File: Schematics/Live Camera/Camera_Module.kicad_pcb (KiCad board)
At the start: 2 copper layers, 69.5 x 60 mm, 96 parts, among them J1 Stack Male Edge Connector, J2 SWD_01x04_Pin, J3 USB_C_Female_USB2_Small, J4 Screw_Terminal_01x02, J5 VTX_DAT, J6 CAM_PWR, J7 CAM_DAT, J8 VTX_PWR, Q1 AO3400A, Q2 AO3401A, Q3 AO3400A, Q4 AO3400A, Q5 AO3401A, SW1 SW_STM_RESET, SW2 SW_STM_BOOT_MODE, U1 LM66100DCKR, U10 AMS1117-3.3, U11 CP2102N-Axx-xQFN28, U2 ACS70331EOLC, U3 STM32F103CBT6, U5 LM66100DCKR, U6 LM66100DCKR, U7 ISO1042BDWVR, U8 W25Q128JVS, Y1 X322516MMB4SI

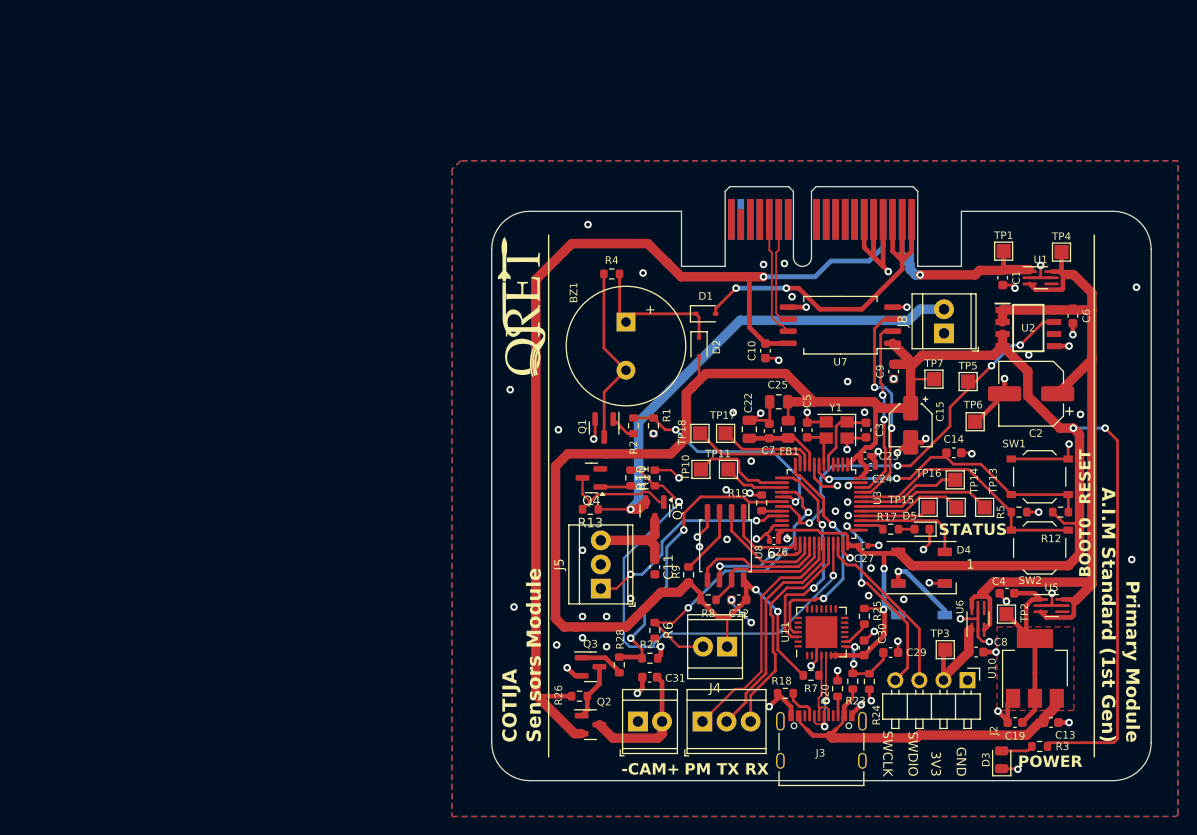
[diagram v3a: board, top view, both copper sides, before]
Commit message: Updated Camera Layout
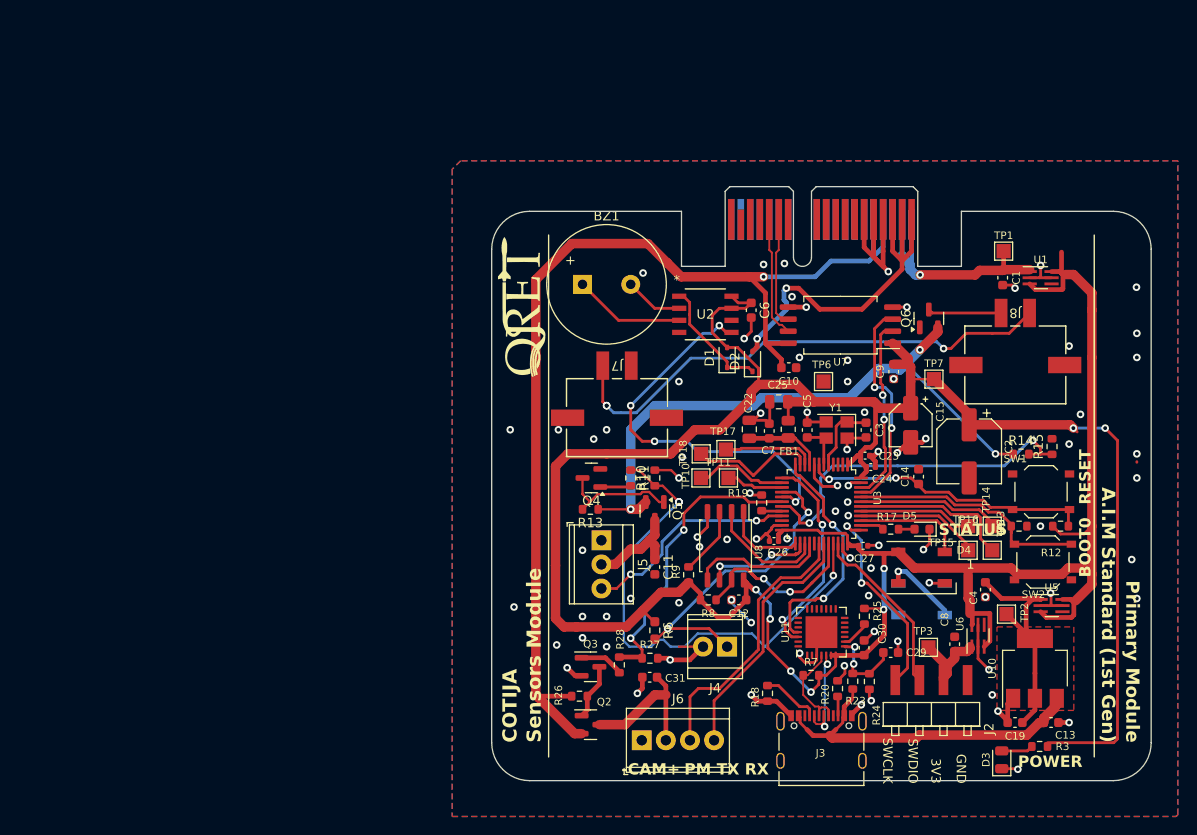
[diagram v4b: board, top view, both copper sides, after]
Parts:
- removed Q1: AO3400A, Package_TO_SOT_SMD:SOT-23
- removed R1: 10k, Resistor_SMD:R_0603_1608Metric
- removed R2: 510R, Resistor_SMD:R_0603_1608Metric
- removed R4: 1k, Resistor_SMD:R_0603_1608Metric
- removed TP4: TP_MUX, TestPoint:TestPoint_Pad_1.5x1.5mm
- removed TP5: TP_ISENSE, TestPoint:TestPoint_Pad_1.5x1.5mm
- added Q6: AO3401A, Package_TO_SOT_SMD:SOT-23, F.Cu at (133.0, 59.4)
- added R14: 100k, Resistor_SMD:R_0603_1608Metric, F.Cu at (142.7, 73.7)
- added R15: 20k, Resistor_SMD:R_0603_1608Metric, F.Cu at (146.0, 72.9)
- BZ1: value PKM13EPYH4000 -> PS1240P02BT
- C6: value 0.1uF -> 100nF
- J2: footprint SWD_Header:SWD_PinHeader_1x04_P2.54mm_Horizontal -> SWD_Header:SWD_PinHeader_1x04_P2.54mm_Horizontal_SMD
- J4: value Screw_Terminal_01x02 -> Therm_In
- J5: value VTX_DAT -> VTX
- J6: value CAM_PWR -> RunCam6; footprint TerminalBlock_TE-Connectivity:TerminalBlock_TE_282834-2_1x02_P2.54mm_Horizontal -> TerminalBlock_TE-Connectivity:TerminalBlock_TE_282834-4_1x04_P2.54mm_Horizontal
- J7: value CAM_DAT -> VTX_BATT_IN; footprint TerminalBlock_TE-Connectivity:TerminalBlock_TE_282834-3_1x03_P2.54mm_Horizontal -> footprints:CONN_2-1445057-2_TYCO
- J8: value VTX_PWR -> VTX_BATT_SWITCH; footprint TerminalBlock_TE-Connectivity:TerminalBlock_TE_282834-2_1x02_P2.54mm_Horizontal -> footprints:CONN_2-1445057-2_TYCO
- R11: value 820 -> 510
- R6: footprint Resistor_SMD:R_0603_1608Metric -> Resistor_SMD:R_0603_1608Metric_Pad0.98x0.95mm_HandSolder
- U2: value ACS70331EOLC -> TPM8837C-SO1R; footprint footprints:SOIC127P600X175-8N -> footprints:SOP-8_TPK
- moved J7 38.2 mm to (101.7, 64.4), turned to 180 degrees
- moved U2 34.1 mm to (109.5, 59.0)
- moved C6 33.9 mm to (114.3, 58.5)
- moved TP6 16.5 mm to (121.9, 66.0)
- moved J8 9.26 mm to (143.6, 58.8), turned to 180 degrees
- moved C2 8.92 mm to (137.3, 73.4), turned to -90 degrees
- moved BZ1 6.44 mm to (95.2, 55.8), turned to 0 degrees
- moved TP16 6.25 mm to (139.7, 81.3)
- moved TP15 6.18 mm to (137.2, 83.8)
- moved D2 5.84 mm to (114.4, 63.9), turned to 90 degrees
- moved D1 5.13 mm to (111.8, 63.5), turned to 90 degrees
- moved J5 5.09 mm to (98.5, 82.8), turned to -90 degrees
- moved TP13 4.59 mm to (139.7, 83.8)
- moved C14 4.48 mm to (131.9, 76.1), turned to 90 degrees
- moved C10 3.03 mm to (118.3, 64.6), turned to 180 degrees
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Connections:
- C11 pad 1: VTX_BAT -> VTX_V+
- C12 pad 1: +3.3V -> V_MUX
- C15 pad 1: +3.3V -> V_MUX
- C23 pad 1: +3.3V -> V_MUX
- C24 pad 1: +3.3V -> V_MUX
- C25 pad 1: +3.3V -> V_MUX
- C26 pad 1: +3.3V -> V_MUX
- C27 pad 1: +3.3V -> V_MUX
- C30 pad 2: +3.3V -> V_MUX
- C9 pad 2: +3.3V -> V_MUX
- D1 pad 1: Net-(BZ1--) -> Net-(D1-K)
- D1 pad 2: +BATT -> V_MUX
- D2 pad 1: Net-(BZ1--) -> Net-(D1-K)
- D2 pad 2: +3.3V -> +BATT
- D4 pad 1: +3.3V -> V_MUX
- D6 pad 1: +3.3V -> V_MUX
- FB1 pad 2: +3.3V -> V_MUX
- J4 pad 1: +3.3V -> V_THERM
- J4 pad 2: V_THERM -> GND
- J5 pad 1: VTX_DATA -> GND
- J5 pad 2: GND -> VTX_V+
- J5 pad 3: VTX_BAT -> VTX_DATA
- J7 pad 1: CAM_TX -> GND
- J7 pad 2: CAM_RX -> Net-(J7-Pad2)
- J8 pad 1: GND -> Net-(J7-Pad2)
- J8 pad 2: VTX_8V -> Net-(Q6-D)
- Q5 pad 2: VTX_8V -> VTX_BATT
- Q5 pad 3: VTX_BAT -> VTX_V+
- R12 pad 2: +3.3V -> V_MUX
- R13 pad 1: VTX_8V -> VTX_BATT
- R25 pad 2: +3.3V -> V_MUX
- R3 pad 2: +3.3V -> V_MUX
- R6 pad 1: V_THERM -> V_MUX
- R6 pad 2: GND -> V_THERM
- R7 pad 1: +3.3V -> V_MUX
- R8 pad 2: +3.3V -> V_MUX
- R9 pad 2: +3.3V -> V_MUX
- SW2 pad 2: +3.3V -> V_MUX
- TP7 pad 1: +3.3V -> V_MUX
- U11 pad 6: +3.3V -> V_MUX
- U11 pad 7: +3.3V -> V_MUX
- U2 pad 1: V_MUX -> Net-(D1-K)
- U2 pad 2: V_MUX -> Net-(BZ1-+)
- U2 pad 3: +3.3V -> Net-(BZ1--)
- U2 pad 4: +3.3V -> GND
- U2 pad 5: GND -> BUZZER_B
- U2 pad 6: unconnected-(U2-NC-Pad6) -> BUZZER_A
- U2 pad 7: CURR_SENSE -> V_MUX
- U3 pad 1: +3.3V -> V_MUX
- U3 pad 17: BUZZER -> BUZZER_B
- U3 pad 19: CURR_SENSE -> VTX_BATT_SENSE
- U3 pad 24: +3.3V -> V_MUX
- U3 pad 29: RESET_FL -> BUZZER_A
- U3 pad 32: CAM_PWM -> RESET_FL
- U3 pad 36: +3.3V -> V_MUX
- U3 pad 48: +3.3V -> V_MUX
- U7 pad 1: +3.3V -> V_MUX
- U8 pad 8: +3.3V -> V_MUX
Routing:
- net +3.3V: track 277.0 -> 0.00 mm, vias 6 -> 0
- net V_MUX: track 87.1 -> 340.1 mm, vias 0 -> 8
- net VTX_BATT: track 0.00 -> 66.6 mm, vias 0 -> 5
- net Net-(J7-Pad2): track 0.00 -> 54.2 mm, vias 0 -> 3
- net VTX_8V: track 52.0 -> 0.00 mm, vias 1 -> 0
- net CURR_SENSE: track 42.9 -> 0.00 mm, vias 4 -> 0
- net BUZZER_B: track 0.00 -> 41.2 mm, vias 0 -> 4
- net VTX_BATT_SENSE: track 0.00 -> 37.8 mm, vias 0 -> 2
- net BUZZER: track 24.4 -> 0.00 mm, vias 2 -> 0
- net CAM_PWM: track 23.6 -> 0.00 mm
- net GND: track 134.5 -> 121.3 mm, vias 84 -> 82
- net Net-(BZ1-+): track 19.1 -> 6.15 mm
- net Net-(D1-K): track 0.00 -> 12.7 mm
- net VTX_BAT: track 11.8 -> 0.00 mm
- net VTX_V+: track 0.00 -> 10.8 mm
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
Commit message: Tweaks + 3D model additions
Added/tweaked some notes in the schematic, adjusted silkscreen on PCB + added "PB-FREE" label, updated SWD footprint, and added all missing 3D models to project.
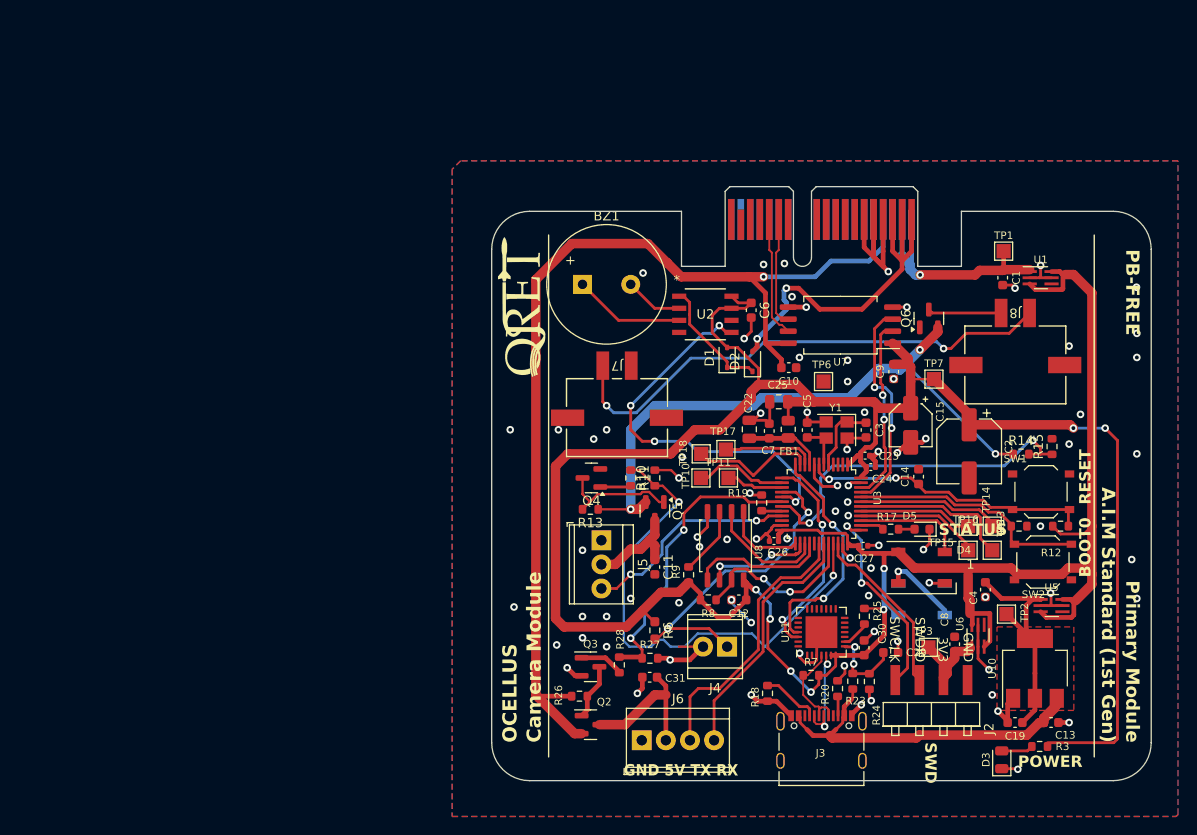
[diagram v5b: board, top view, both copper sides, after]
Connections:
- net 5V_RAW renamed 5V_USB
- net V_MUX renamed +3.3V
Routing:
- net +3.3V: track 340.1 -> 336.3 mm
- net RESET_FL: track 19.0 -> 18.4 mm
- net VTX_PWR: vias 4 -> 2
- net VTX_BATT: vias 5 -> 3
- net Net-(J7-Pad2): vias 3 -> 2
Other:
- board text added: "Camera Module"
- board text added: "GND 5V TX RX"
- board text added: "OCELLUS"
- board text added: "Ocellus Rev 1.0 QRET Feb 2025 Ethan Toste Kennan Bays Noah Del Rizzo Fedor Kim"
- board text added: "PB-FREE"
- board text removed: "-CAM+"
- board text removed: "?????? Rev 1.0 QRET Feb 2025 Ethan Toste Kennan Bays Noah Del Rizzo Fedor Kim"
- board text removed: "COTIJA"
- board text removed: "JLCJLCJLCJLC"
- board text removed: "PM TX RX"
- board text removed: "Sensors Module"

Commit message: Refined & finalized PCB layout
Moved connectors all to the edge of the PCB to make access easier, beefed up several traces, optimized trace paths to minimize traces on the rear ground plane. Removed a few redundant test points too.
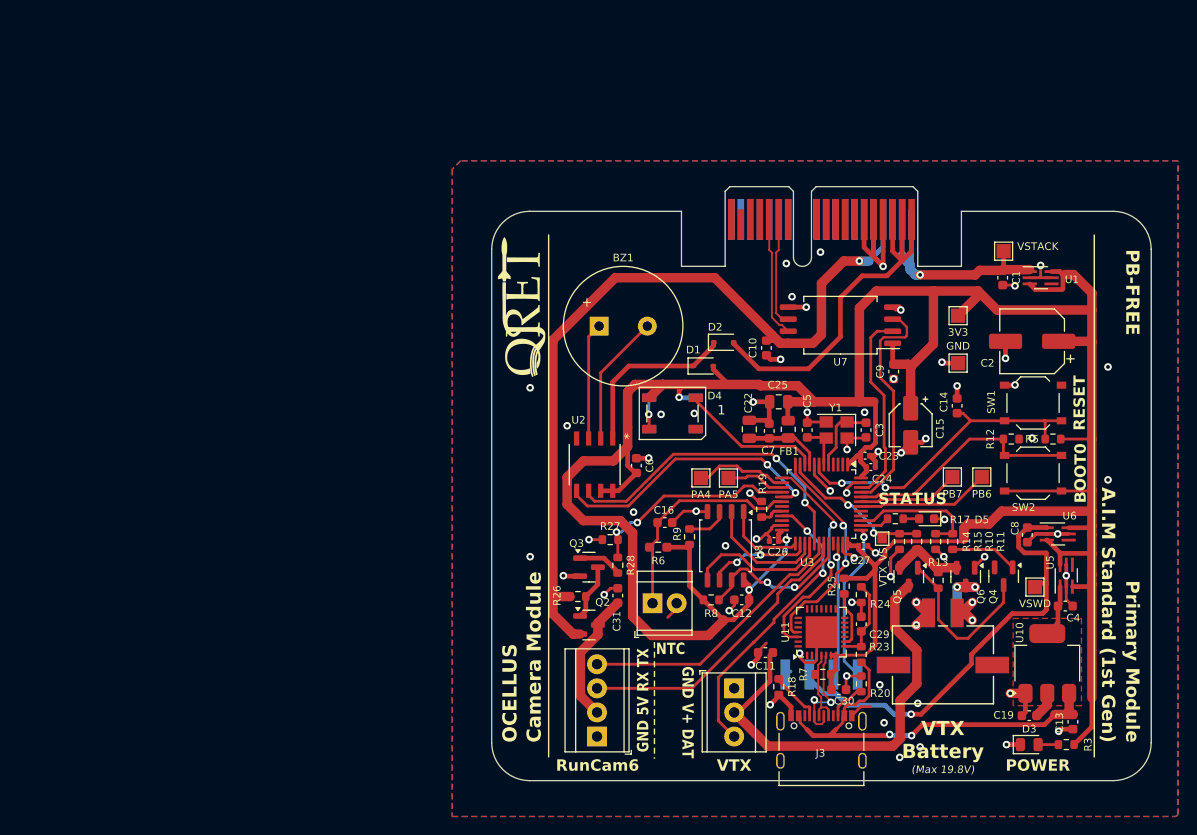
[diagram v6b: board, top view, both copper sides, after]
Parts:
- removed TP14: PB5, TestPoint:TestPoint_Pad_1.5x1.5mm
- removed TP15: PB4, TestPoint:TestPoint_Pad_1.5x1.5mm
- removed TP17: PA0, TestPoint:TestPoint_Pad_1.5x1.5mm
- removed TP18: PA1, TestPoint:TestPoint_Pad_1.5x1.5mm
- added C16: 100nF, Capacitor_SMD:C_0603_1608Metric, F.Cu at (105.2, 80.9)
- J2, J8: moved to B.Cu
- TP1: value TP_VSTACK -> VSTACK
- TP2: value TP_VUSB -> VTX_VS; footprint TestPoint:TestPoint_Pad_1.5x1.5mm -> TestPoint:TestPoint_Pad_1.0x1.0mm
- TP3: value TP_VSWD -> VSWD
- TP6: value TP_GND -> GND
- TP7: value TP_3V3 -> 3V3
- moved Q4 44.7 mm to (140.9, 86.6), turned to -90 degrees
- moved J7 43.1 mm to (136.0, 90.4)
- moved R13 37.4 mm to (134.0, 87.0), turned to -90 degrees
- moved R11 34.6 mm to (135.5, 82.9)
- moved J8 33.4 mm to (133.0, 90.4), turned to 0 degrees
- moved D6 32.8 mm to (106.0, 69.4), turned to 180 degrees
- moved D4 30.9 mm to (106.0, 69.4)
- moved R10 30.3 mm to (133.7, 82.9), turned to -90 degrees
- moved Q5 27.6 mm to (130.9, 86.6)
- moved Q6 27.5 mm to (136.9, 86.6), turned to -90 degrees
- moved J5 21.0 mm to (112.5, 98.4)
- moved C6 20.4 mm to (102.2, 74.9), turned to 90 degrees
- moved U2 19.7 mm to (97.8, 74.8), turned to -90 degrees
- moved J2 19.2 mm to (117.9, 96.9)
- moved R15 18.9 mm to (129.9, 82.9), turned to -90 degrees
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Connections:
- J6 pad 3: CAM_TX -> CAM_RX
- J6 pad 4: CAM_RX -> CAM_TX
- TP2 pad 1: V_REGUSB -> VTX_BATT_SENSE
- U3 pad 10: Net-(U3-PA0) -> RGB_DATA
- U3 pad 11: Net-(U3-PA1) -> VTX_BATT_SENSE
- U3 pad 16: V_THERM -> CAM_PWR
- U3 pad 18: CAM_PWR -> V_THERM
- U3 pad 19: VTX_BATT_SENSE -> unconnected-(U3-PB1-Pad19)
- U3 pad 33: VTX_PWR -> unconnected-(U3-PA12-Pad33)
- U3 pad 39: RGB_DATA -> VTX_PWR
- U3 pad 40: Net-(U3-PB4) -> unconnected-(U3-PB4-Pad40)
- U3 pad 41: Net-(U3-PB5) -> unconnected-(U3-PB5-Pad41)
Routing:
- net VTX_BATT: track 66.6 -> 7.59 mm, vias 3 -> 0
- net Net-(J7-Pad2): track 54.2 -> 7.20 mm
- net VTX_PWR: track 54.2 -> 13.9 mm, vias 2 -> 0
- net V_SWD: track 8.23 -> 47.2 mm, vias 0 -> 1
- net VTX_V+: track 10.8 -> 46.0 mm
- net BUZZER_A: track 0.00 -> 33.4 mm, vias 0 -> 2
- net +5V: track 114.9 -> 90.5 mm
- net VTX_BATT_SENSE: track 37.8 -> 16.1 mm
- net V_REGUSB: track 25.7 -> 8.33 mm
- net Net-(U3-PA1): track 13.3 -> 0.00 mm
- net Net-(U3-PB4): track 13.1 -> 0.00 mm
- net BUZZER_B: track 41.2 -> 29.1 mm, vias 4 -> 2
- net Net-(U3-PB5): track 12.0 -> 0.00 mm
- net V_THERM: track 33.9 -> 23.7 mm, vias 2 -> 0
- net Net-(U3-PA0): track 9.69 -> 0.00 mm
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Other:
- board text added: "(Max 19.8V)"
- board text added: "GND 5V RX TX"
- board text added: "GND V+ DAT"
- board text added: "NTC"
- board text added: "RunCam6"
- board text added: "VTX"
- board text added: "VTX Battery"
- board text added: "VTX Switch"
- board text removed: "GND 5V TX RX"

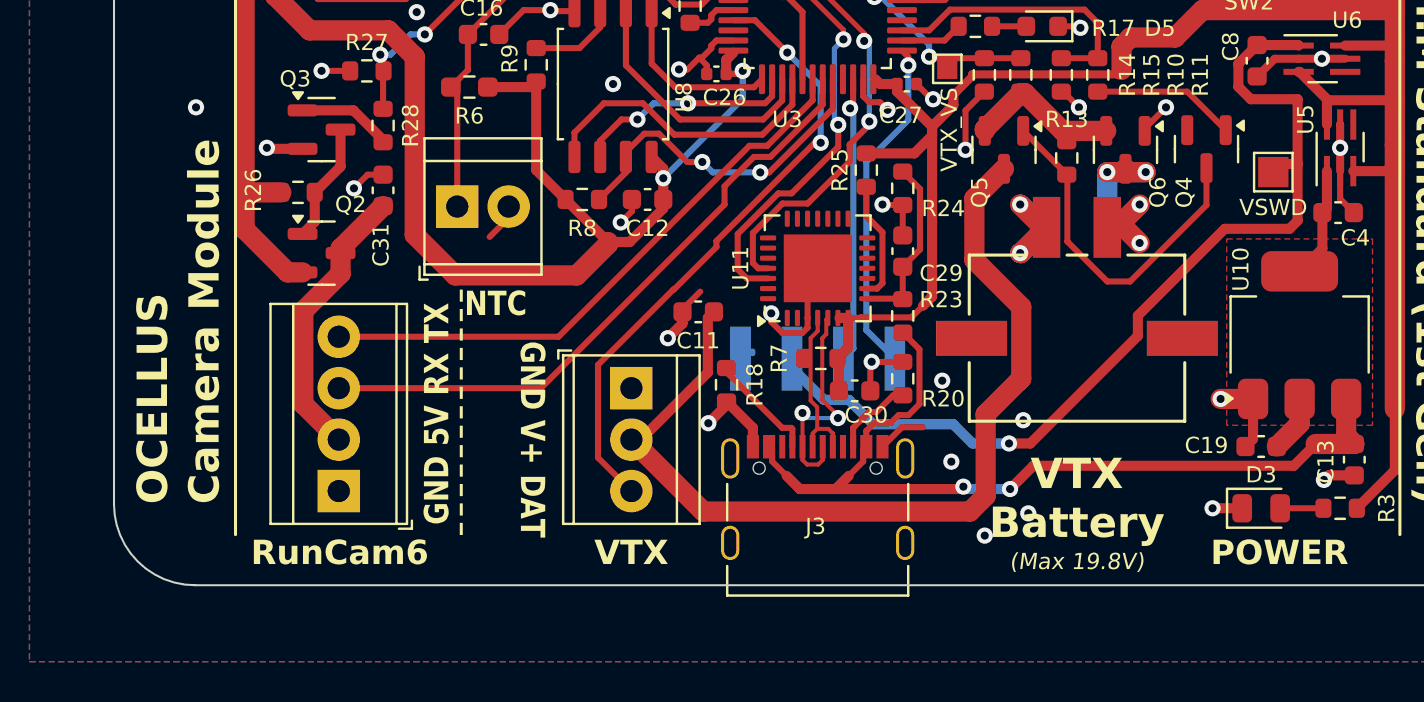
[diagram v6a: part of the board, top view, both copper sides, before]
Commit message: Quick maintenance
- Changed USB-C port to new one (C5178541)
- Moved VTX battery/switch connectors 4mm forward
- Added polarity markers to VTX battery/switch connectors
- Tweaked silkscreen
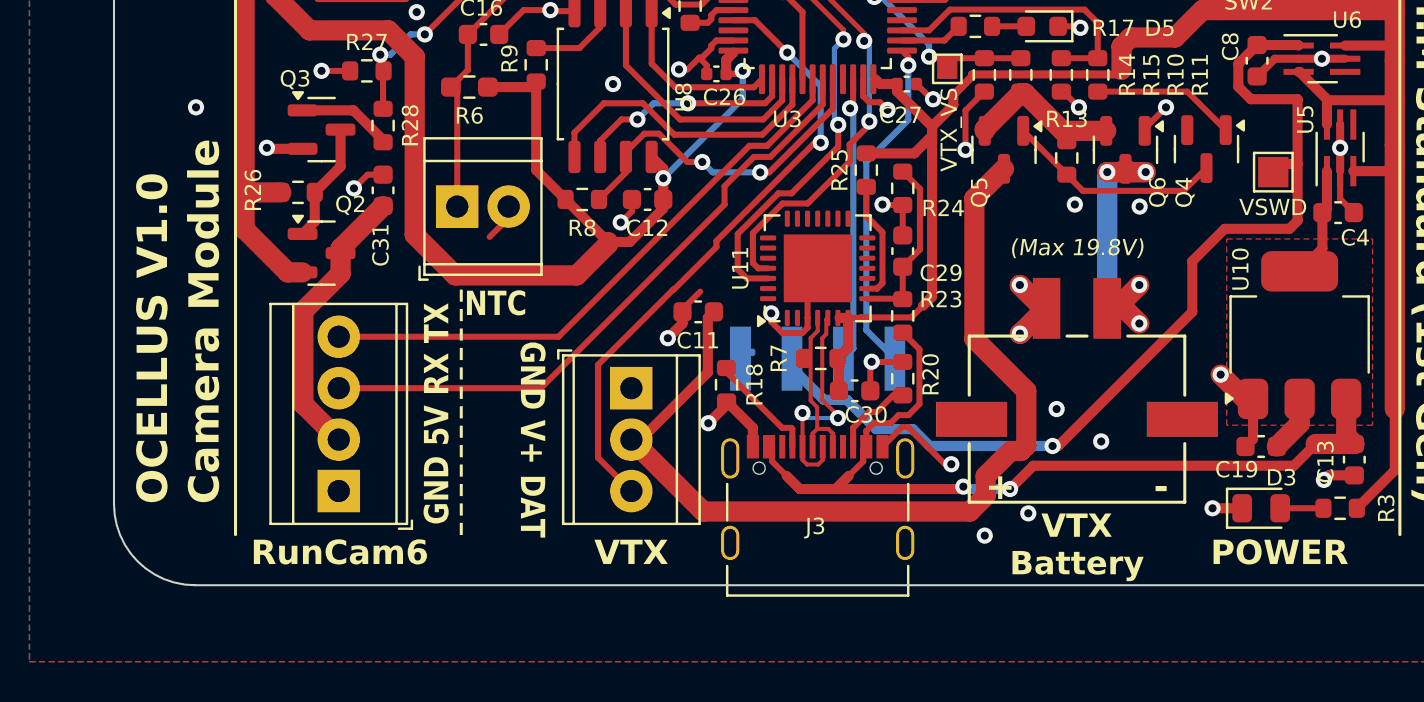
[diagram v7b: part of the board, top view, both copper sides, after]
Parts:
- moved J7 4.00 mm to (136.0, 94.4)
- moved J8 4.00 mm to (133.0, 94.4)
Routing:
- net Net-(Q4-D): track 17.4 -> 10.8 mm
- net Net-(Q6-D): track 6.66 -> 10.7 mm
- net GND: track 128.1 -> 130.8 mm, vias 64 -> 66
- net V_SWD: track 47.2 -> 48.1 mm
- net VTX_V+: track 46.0 -> 46.5 mm
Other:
- board text added: "+ -"
- board text added: "- +"
- board text added: "OCELLUS V1.0"
- board text added: "Ocellus Rev 1.0 QRET Mar 2025 Ethan Toste Kennan Bays Noah Del Rizzo Fedor Kim"
- board text removed: "OCELLUS"
- board text removed: "Ocellus Rev 1.0 QRET Feb 2025 Ethan Toste Kennan Bays Noah Del Rizzo Fedor Kim"
